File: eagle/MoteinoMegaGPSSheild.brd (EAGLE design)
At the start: 59.4 x 34.3 mm, 24 parts, among them J1 BilgeSwitch, J2 Button, J3 LED, J4 DS18B20, J5 DS18B20, J6 5V_GDN, J7 OKI-78SR-5/1.5, J8 5V, J9 12-24V_VCC, Q1 NDP6020P P-CHANNEL, Q2 IRF9Z14PBF, Q3 2N7000

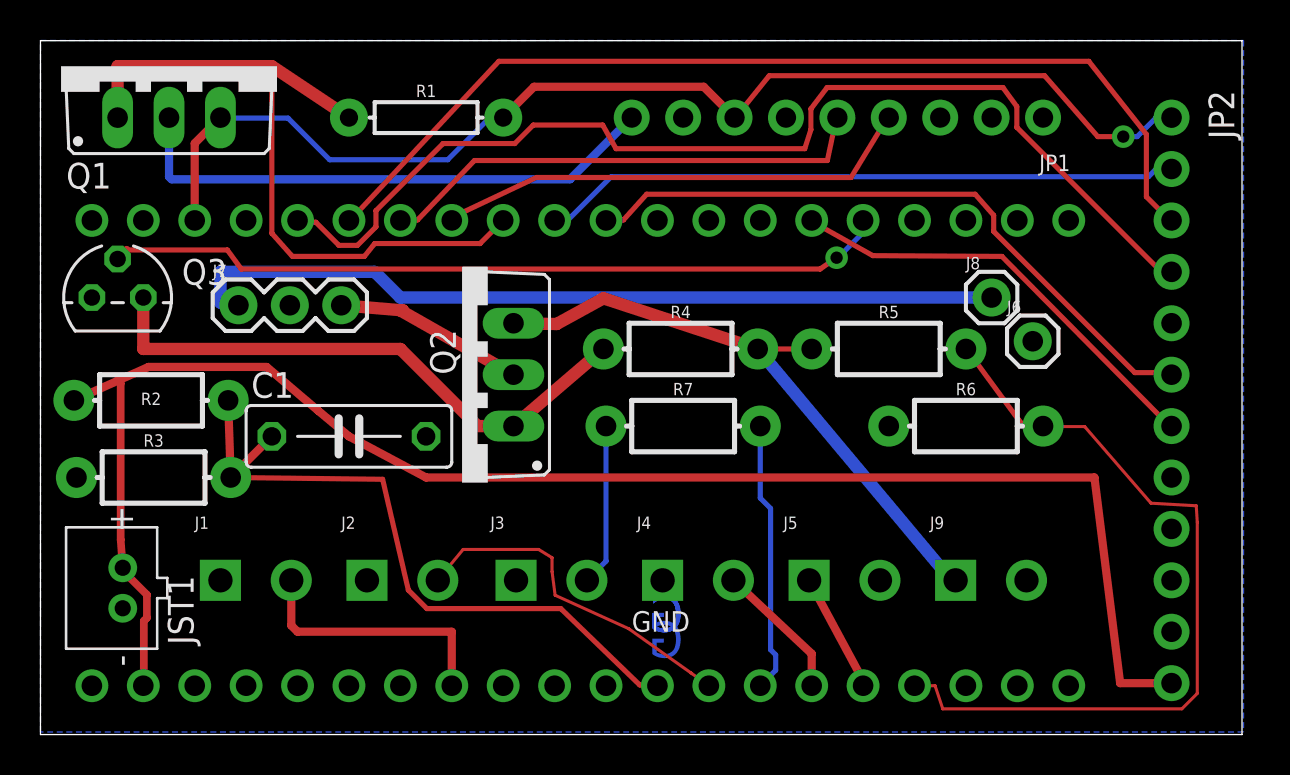
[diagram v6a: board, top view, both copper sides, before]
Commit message: V0.91.  Changed netclasses, autorouted, tidied names.  Bar one Width and a few angle errors passes sparkfun and oshpark DRC rules
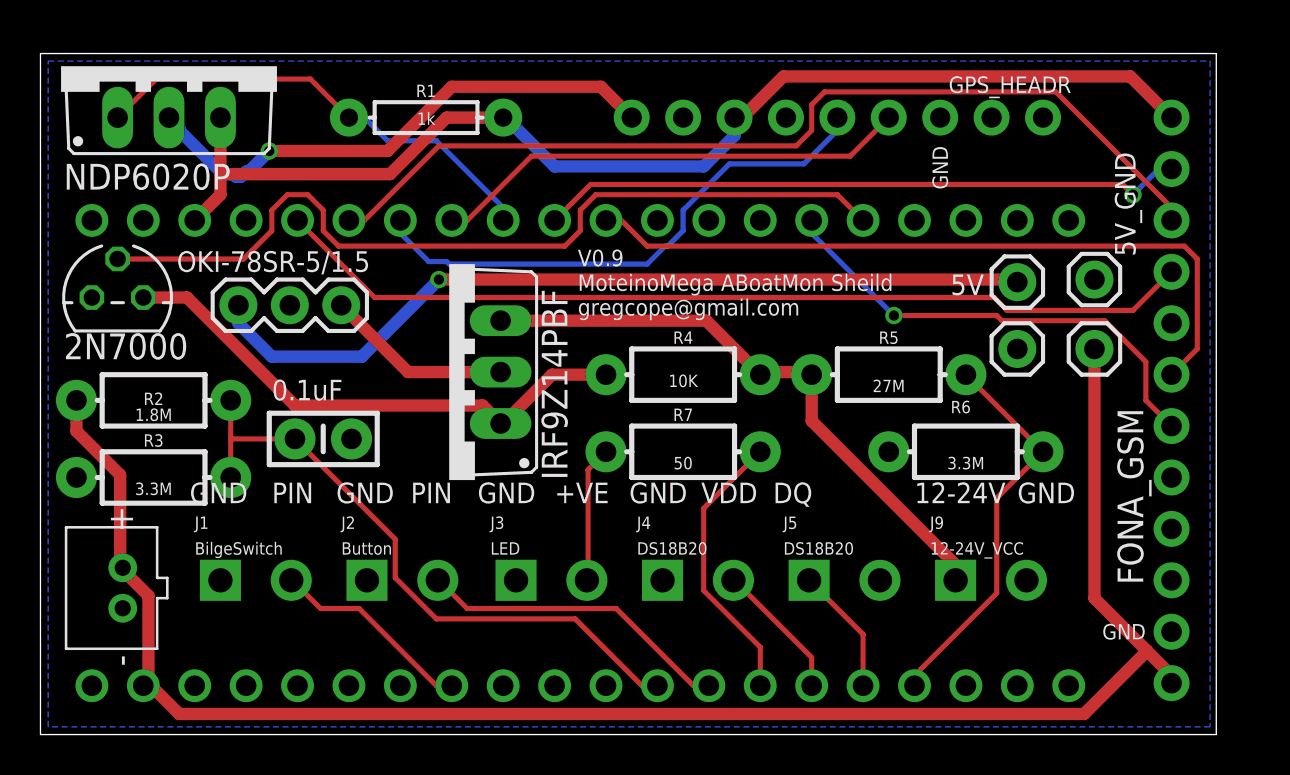
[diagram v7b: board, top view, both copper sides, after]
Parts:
- added J10: LIPO_VCC, SparkFun-Connectors:1X01
- added J11: LIPO_GND, SparkFun-Connectors:1X01
- C1: value 0.1uF -> 0.1UF-KIT-EZ-50V-20%; device adafruit:C075-032X103 -> SparkFun-Capacitors:CAP-PTH-SMALL-KIT
- J6: value 5V_GDN -> 5V_GND
- Q1: value NDP6020P P-CHANNEL -> NDP6020P
- moved J6 4.31 mm to (52.1, 51.7)
- moved J8 1.48 mm to (48.3, 51.6)
- moved C1 1.28 mm to (14.0, 43.8)
- moved R4 1.28 mm to (31.8, 47.0)
- moved R6 1.27 mm to (45.7, 43.2)
- moved R7 1.27 mm to (31.8, 43.2)
- moved R5 1.27 mm to (41.9, 47.0)
- moved Q2 0.65 mm to (20.2, 47.1)
- moved R2 0.13 mm to (5.59, 45.7)
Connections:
- net GND: now also J11.1
- net VIN: now also J10.1
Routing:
- net A5: track 39.5 -> 19.6 mm
- net D12: track 35.7 -> 23.1 mm
- net D8: track 54.0 -> 45.8 mm
- net VIN: track 81.0 -> 85.2 mm
- net D19_PWRON: track 38.8 -> 42.6 mm, vias 1 -> 0
- net D14_KEY: track 32.7 -> 36.2 mm
- net A0: track 34.0 -> 31.1 mm
- net D3: track 13.0 -> 10.1 mm
- net D9: track 49.4 -> 47.0 mm
- net D10_RX1: track 24.6 -> 26.8 mm
- net N$2: track 28.3 -> 26.4 mm
- net D18_PS: track 21.7 -> 23.5 mm, vias 0 -> 1
- net D25: track 17.2 -> 15.5 mm
- net N$7: track 8.01 -> 6.77 mm
- net 12-24V-VCC: track 30.5 -> 29.6 mm
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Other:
- board size 59.4 x 34.3 mm -> 58.1 x 33.6 mm
- board text added: "+VE"
- board text added: "0.1uF"
- board text added: "12-24V"
- board text added: "DQ"
- board text added: "PIN"
- board text added: "V0.9 MoteinoMega ABoatMon Sheild gregcope@gmail.com"
- board text added: "VDD"
- board text removed: "G"

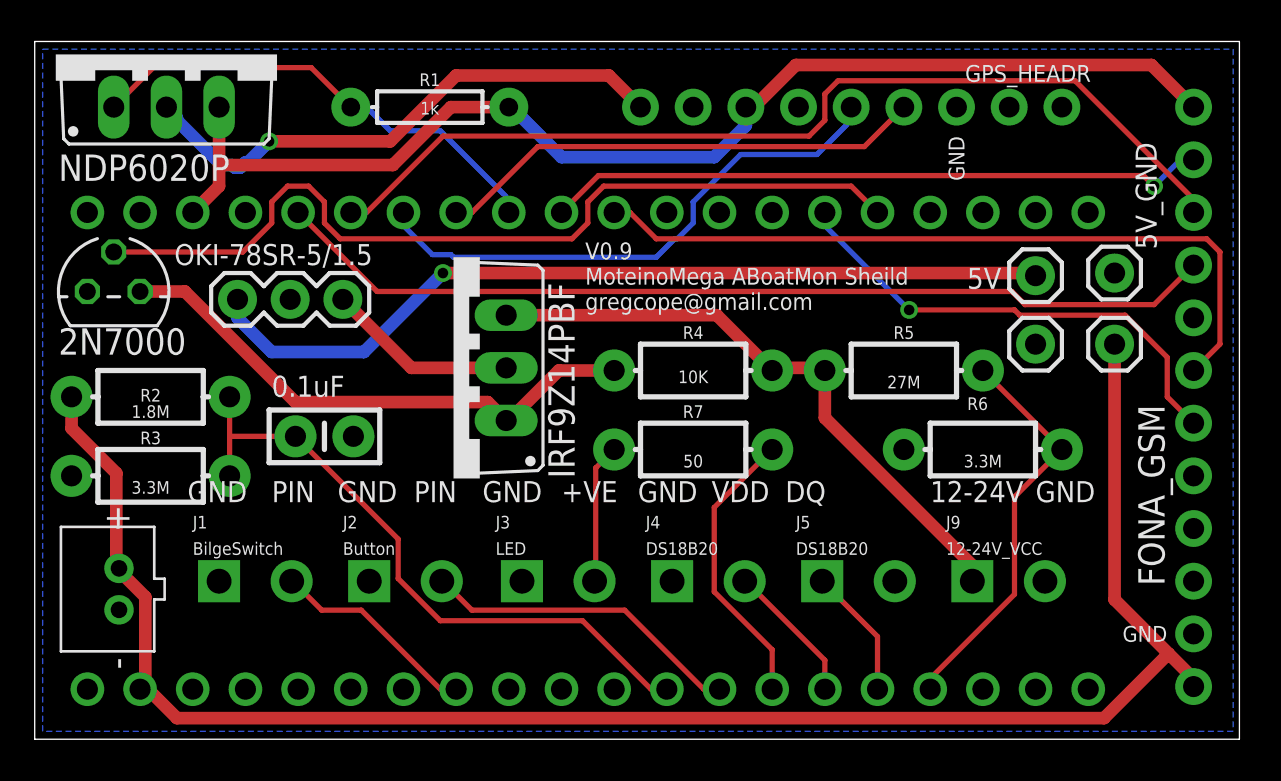
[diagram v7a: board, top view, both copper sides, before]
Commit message: V0.97 - Silkscreen fixes
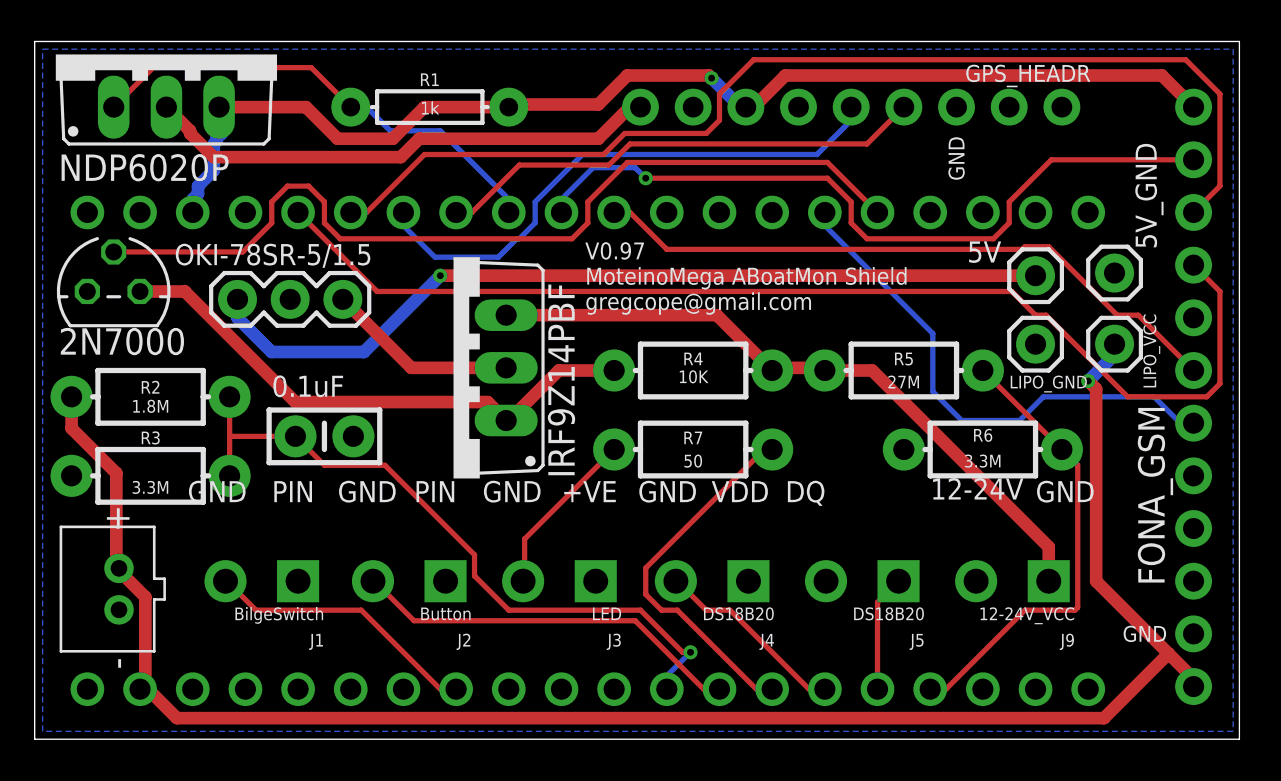
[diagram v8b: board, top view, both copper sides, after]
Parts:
- moved J1 3.81 mm to (12.7, 36.8), turned to 180 degrees
- moved J2 3.68 mm to (19.8, 36.8), turned to 180 degrees
- moved J4 3.68 mm to (34.4, 36.8), turned to 180 degrees
- moved J5 3.68 mm to (41.7, 36.8), turned to 180 degrees
- moved J9 3.68 mm to (48.9, 36.8), turned to 180 degrees
- moved J3 3.56 mm to (27.1, 36.8), turned to 180 degrees
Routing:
- net D8: track 45.8 -> 54.6 mm
- net D9: track 47.0 -> 52.6 mm
- net D14_KEY: track 36.2 -> 31.2 mm
- net D13_NETSTAT: track 32.0 -> 35.9 mm
- net D26: track 13.9 -> 17.7 mm
- net D25: track 15.5 -> 18.9 mm
- net D3: track 10.1 -> 13.3 mm
- net 12-24V-VCC: track 29.6 -> 32.5 mm
- net D27: track 6.84 -> 9.34 mm
- net A5: track 19.6 -> 22.1 mm
- net A0: track 31.1 -> 33.2 mm, vias 0 -> 1
- net GPS_VCC: track 26.6 -> 24.9 mm, vias 1 -> 0
- net 3.3V: track 58.1 -> 56.5 mm, vias 0 -> 1
- net D18_PS: track 23.5 -> 24.9 mm, vias 1 -> 0
- net N$7: track 6.77 -> 8.21 mm
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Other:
- board text added: "V0.97 MoteinoMega ABoatMon Shield gregcope@gmail.com"
- board text removed: "V0.9 MoteinoMega ABoatMon Sheild gregcope@gmail.com"
